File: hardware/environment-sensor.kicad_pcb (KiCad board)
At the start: 2 copper layers, 111 x 86 mm, 109 parts, among them P2 ICSP, P4 JTAG, P5 RB1-125BAG1A, P6 NSL-19M51, P7 PPD42, P8 POWER, SW1 Reset, U1 ATMEGA32U4-AU, U2 W5500, U3 Bosch_BME280, U4 LM317T, U5 LM317T, X1 16MHz, X2 25MHz

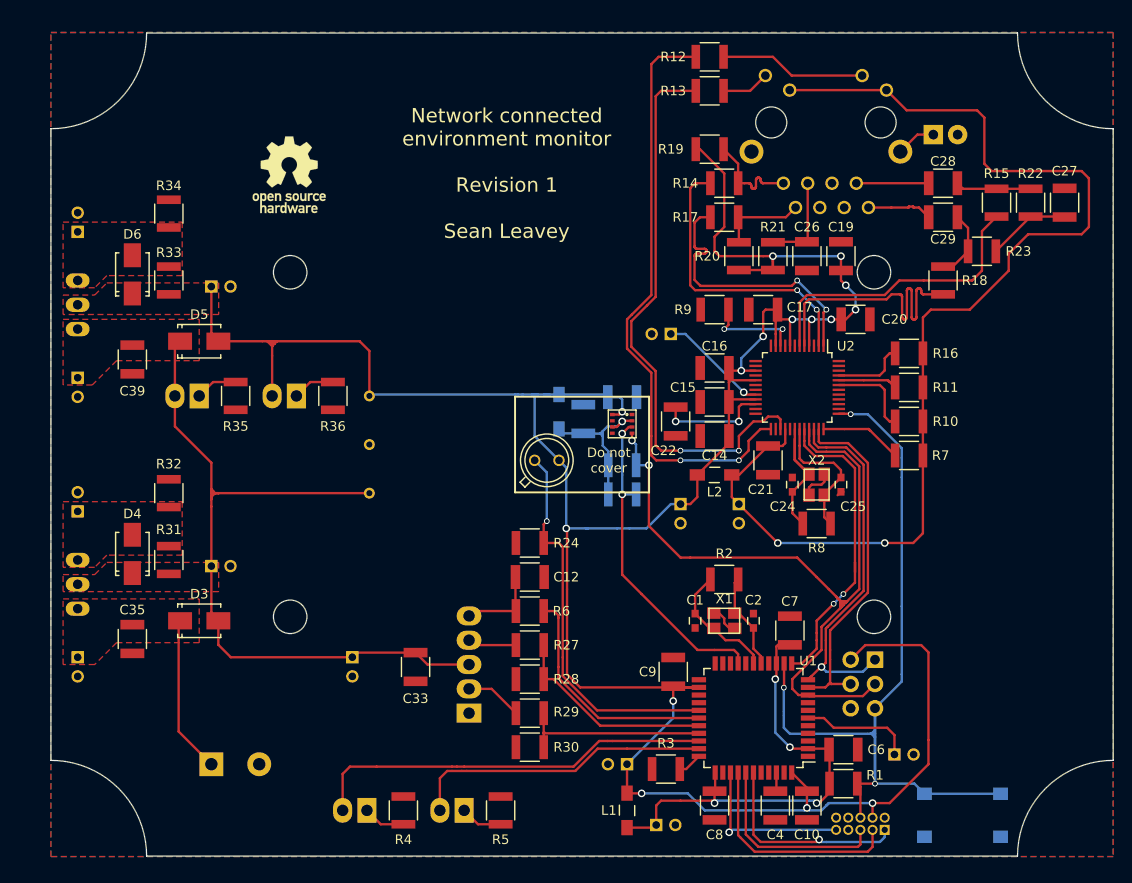
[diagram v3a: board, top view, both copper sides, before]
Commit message: Revision of board to address issues
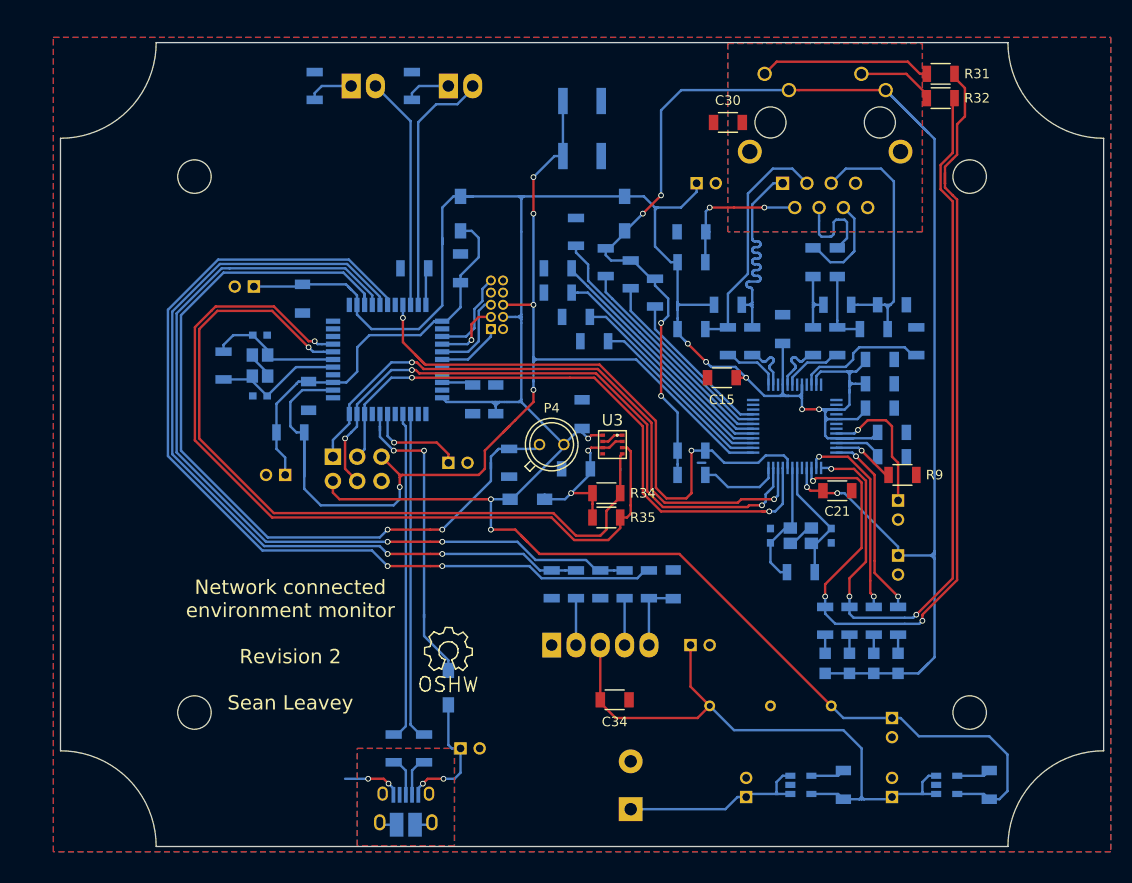
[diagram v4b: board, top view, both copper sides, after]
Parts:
- removed C40, C41: 10u, Capacitors_ThroughHole:C_Radial_D5_L11_P2
- removed D7: LED_5V, Connectors_Molex:Molex_KK-6410-02_02x2.54mm_Straight
- removed D8: LED_3V3, Connectors_Molex:Molex_KK-6410-02_02x2.54mm_Straight
- removed JP1: Shield ground, Pin_Headers:Pin_Header_Straight_1x02
- removed P7: PPD42, Connectors_Molex:Molex_KK-6410-05_05x2.54mm_Straight
- removed P8: POWER, Terminal_Blocks:TerminalBlock_Pheonix_MKDS1.5-2pol
- removed REF*** (x2): OSHW-Logo_7.5x8mm_SilkScreen, Symbols:OSHW-Logo_7.5x8mm_SilkScreen
- removed the Ref** at (156.8, 101.0)
- added J1: J1B1211CCD, Cetus_RJ45:Cetus_J1B1211CCD, B.Cu at (182.2, 67.3)
- added L4: Wurth WE-CBF, Choke_SMD:Choke_SMD_1206_Standard, B.Cu at (151.1, 106.7)
- added P1: USB_OTG, Connect:USB_Micro-B_10103594-0001LF, B.Cu at (138.4, 139.1)
- added P3: JTAG, Pin_Headers:Pin_Header_Straight_2x05_Pitch1.27mm, B.Cu at (147.3, 88.9)
- added R37: 10k, Resistors_SMD:R_1206, B.Cu at (158.8, 115.6)
- added R38: 10k, Resistors_SMD:R_1206, B.Cu at (156.2, 115.6)
- added R39: 10k, Resistors_SMD:R_1206, B.Cu at (153.7, 115.6)
- added R40: 330R, Resistors_SMD:R_1206, B.Cu at (184.8, 119.4)
- added R41: 330R, Resistors_SMD:R_1206, B.Cu at (189.9, 119.4)
- added R42: 330R, Resistors_SMD:R_1206, B.Cu at (187.3, 119.4)
- added R43: 330R, Resistors_SMD:R_1206, B.Cu at (182.2, 119.4)
- added REF**: Symbol_OSHW-Logo_SilkScreen, Symbols:Symbol_OSHW-Logo_SilkScreen, F.Cu at (142.9, 122.6)
- added Ref**: Val**, Board_Outlines:109mmx84mm_holes_b, F.Cu at (156.8, 101.0)
- C1: value 12p -> 10u; footprint Capacitors_SMD:C_0603 -> Capacitors_ThroughHole:C_Radial_D5_L11_P2; moved to B.Cu
- C10, C12, C14, C16, C17, C19, C20, C22, C27, C7, C8, C9: footprint Capacitors_SMD:C_1210 -> Capacitors_SMD:C_1206; moved to B.Cu
- C15, C21, C31: footprint Capacitors_SMD:C_1210 -> Capacitors_SMD:C_1206
- C2, L1, L2, U1, U2, X1, X2: moved to B.Cu
- C24, C25: value 12p -> 10p; moved to B.Cu
- C26: value 100n -> 22n; footprint Capacitors_SMD:C_1210 -> Capacitors_SMD:C_1206; moved to B.Cu
- C28, C29: value 10n -> 6.8n; footprint Capacitors_SMD:C_1210 -> Capacitors_SMD:C_1206; moved to B.Cu
- C3: value 10u -> 12p; footprint Capacitors_ThroughHole:C_Radial_D5_L11_P2 -> Capacitors_SMD:C_0603
- C30: value 100n -> 1n/2kV; footprint Capacitors_SMD:C_1210 -> Capacitors_SMD:C_1206; moved to F.Cu
- C32, C5: value 10u -> 100n; footprint Capacitors_ThroughHole:C_Radial_D5_L11_P2 -> Capacitors_SMD:C_1206
- C33, C35, C39, C6: value 100n -> 10u; footprint Capacitors_SMD:C_1210 -> Capacitors_ThroughHole:C_Radial_D5_L11_P2; moved to B.Cu
- C34: value 10u -> 100n; footprint Capacitors_ThroughHole:C_Radial_D5_L11_P2 -> Capacitors_SMD:C_1206; moved to F.Cu
- C36, C38: value 10u -> 10n; footprint Capacitors_ThroughHole:C_Radial_D5_L11_P2 -> Capacitors_SMD:C_1206
- C4: value 100n -> 1u; footprint Capacitors_SMD:C_1210 -> Capacitors_ThroughHole:C_Radial_D5_L11_P2; moved to B.Cu
- D3: value S1B-13-F -> LINKLED; footprint Diodes_SMD:SMA_Standard -> LEDs:LED_0805; moved to B.Cu
- D4: value S1B-13-F -> SPDLED; footprint Diodes_SMD:SMA_Standard -> LEDs:LED_0805; moved to B.Cu
- D5: value S1B-13-F -> DUPLED; footprint Diodes_SMD:SMA_Standard -> LEDs:LED_0805; moved to B.Cu
- D6: value S1B-13-F -> ACTLED; footprint Diodes_SMD:SMA_Standard -> LEDs:LED_0805; moved to B.Cu
- P4: value JTAG -> NSL-19M51; footprint Pin_Headers:Pin_Header_Straight_2x05_Pitch1.27mm -> TO_SOT_Packages_THT:TO-18_2Pin; moved to F.Cu
- P5: value RB1-125BAG1A -> PPD42; footprint Wiznet_RJ45:WIZNET_RB1-125BAG1A -> Connectors_Molex:Molex_KK-6410-05_05x2.54mm_Straight
- P6: value NSL-19M51 -> POWER; footprint TO_SOT_Packages_THT:TO-18_2Pin -> Terminal_Blocks:TerminalBlock_Pheonix_MKDS1.5-2pol; moved to B.Cu
- R1, R10, R11: footprint Resistors_SMD:R_1210 -> Resistors_SMD:R_1206; moved to B.Cu
- R12: value 330R -> 1M; footprint Resistors_SMD:R_1210 -> Resistors_SMD:R_1206; moved to B.Cu
- R13: value 330R -> 12k4/1%; footprint Resistors_SMD:R_1210 -> Resistors_SMD:R_1206; moved to B.Cu
- R14, R15, R18: value 33R -> 10k; footprint Resistors_SMD:R_1210 -> Resistors_SMD:R_1206; moved to B.Cu
- R16, R24: value 10k -> 0R; footprint Resistors_SMD:R_1210 -> Resistors_SMD:R_1206; moved to B.Cu
- R17: value 33R -> 0R; footprint Resistors_SMD:R_1210 -> Resistors_SMD:R_1206; moved to B.Cu
- R19, R20, R22, R23: value 49R9/1% -> 10k; footprint Resistors_SMD:R_1210 -> Resistors_SMD:R_1206; moved to B.Cu
- R2: value 1M -> 22R; footprint Resistors_SMD:R_1210 -> Resistors_SMD:R_1206; moved to B.Cu
- R21: value 10R/1% -> 10k; footprint Resistors_SMD:R_1210 -> Resistors_SMD:R_1206; moved to B.Cu
- R25: value 4k7 -> 0R; footprint Resistors_SMD:R_1210 -> Resistors_SMD:R_1206
- R26: value 4k7 -> 49R9/1%; footprint Resistors_SMD:R_1210 -> Resistors_SMD:R_1206
- R27, R29, R30: value 10k -> 49R9/1%; footprint Resistors_SMD:R_1210 -> Resistors_SMD:R_1206; moved to B.Cu
- R28: value 10k -> 10R/1%; footprint Resistors_SMD:R_1210 -> Resistors_SMD:R_1206; moved to B.Cu
- R3: value 10k -> 22R; footprint Resistors_SMD:R_1210 -> Resistors_SMD:R_1206; moved to B.Cu
- R31: value 110R -> 330R; footprint Resistors_SMD:R_1210 -> Resistors_SMD:R_1206
- R32: footprint Resistors_SMD:R_1210 -> Resistors_SMD:R_1206
- R33: value 110R -> 10k; footprint Resistors_SMD:R_1210 -> Resistors_SMD:R_1206; moved to B.Cu
- R34: value 180R -> 4k7; footprint Resistors_SMD:R_1210 -> Resistors_SMD:R_1206
- R35: value 270R -> 4k7; footprint Resistors_SMD:R_1210 -> Resistors_SMD:R_1206
- R36, R5: value 180R -> 10k; footprint Resistors_SMD:R_1210 -> Resistors_SMD:R_1206; moved to B.Cu
- R4: value 180R -> 1M; footprint Resistors_SMD:R_1210 -> Resistors_SMD:R_1206; moved to B.Cu
- R6, R7: value 10k -> 180R; footprint Resistors_SMD:R_1210 -> Resistors_SMD:R_1206; moved to B.Cu
- R8: value 1M -> 10k; footprint Resistors_SMD:R_1210 -> Resistors_SMD:R_1206; moved to B.Cu
- R9: value 12k4/1% -> 10k; footprint Resistors_SMD:R_1210 -> Resistors_SMD:R_1206
- SW1: footprint Buttons_Switches_SMD:SW_SPST_B3S-1000 -> Buttons_Switches_SMD:SW_SPST_B3SL-1002P
- U4: value LM317T -> LT1761-5; footprint TO_SOT_Packages_THT:TO-220_Neutral123_Vertical -> TO_SOT_Packages_SMD:SOT-23-5
- U5: value LM317T -> LT1761-3.3; footprint TO_SOT_Packages_THT:TO-220_Neutral123_Vertical -> TO_SOT_Packages_SMD:SOT-23-5
- moved C38 104.3 mm to (199.4, 136.5)
- moved U5 103.7 mm to (194.9, 136.5), turned to 0 degrees
- moved R31 95.3 mm to (194.3, 62.2), turned to 0 degrees
- moved R32 90.6 mm to (194.3, 64.8), turned to 0 degrees
- moved C39 87.8 mm to (189.2, 129.5)
- moved C36 85.0 mm to (184.2, 136.5), turned to 270 degrees
- moved D6 83.0 mm to (182.2, 123.8), turned to 270 degrees
- moved SW1 82.0 mm to (156.8, 67.9), turned to 270 degrees
- moved D4 80.8 mm to (189.9, 123.8), turned to 270 degrees
- moved U4 78.4 mm to (179.7, 136.5), turned to 0 degrees
- moved D5 78.1 mm to (187.3, 123.8), turned to 270 degrees
- moved C3 76.1 mm to (123.2, 95.9), turned to 180 degrees
- moved D1 75.7 mm to (132.7, 63.5), turned to 0 degrees
- moved D2 75.7 mm to (142.9, 63.5), turned to 0 degrees
- moved C37 75.1 mm to (189.2, 137.8), turned to 90 degrees
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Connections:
- net /Microcontroller/MISO renamed /Microcontroller/SPI_MISO
- net /Microcontroller/MOSI renamed /Microcontroller/SPI_MOSI
- C30 pad 1: /Microcontroller/3V3A -> GND
- C30 pad 2: GND -> /Network I/O/CHGND
- C31 pad 1: /Sensors/3V3D -> /Microcontroller/3V3A
- C32 pad 1: /Power Supply/5VA -> /Sensors/3V3D
- C33 pad 1: GND -> /Power Supply/5VA
- C33 pad 2: /Power Supply/5VA -> GND
- C34 pad 1: /Power Supply/+6V -> GND
- C34 pad 2: GND -> /Power Supply/5VA
- C36 pad 2: GND -> /Power Supply/5VA
- C38 pad 1: /Power Supply/5VA -> Net-(C38-Pad1)
- C38 pad 2: GND -> /Microcontroller/3V3A
- C39 pad 1: /Power Supply/5VA -> /Microcontroller/3V3A
- C5 pad 1: /Microcontroller/3V3D -> Net-(C5-Pad1)
- C6 pad 1: GND -> /Microcontroller/3V3D
- C6 pad 2: /Microcontroller/3V3D -> GND
- D3 pad 1: /Power Supply/+6V -> Net-(D3-Pad1)
- D3 pad 2: /Power Supply/5VA -> /Network I/O/3V3D
- D4 pad 1: /Power Supply/5VA -> Net-(D4-Pad1)
- D4 pad 2: Net-(C36-Pad1) -> /Network I/O/3V3D
- D5 pad 1: /Power Supply/5VA -> Net-(D5-Pad1)
- D5 pad 2: /Microcontroller/3V3A -> /Network I/O/3V3D
- D6 pad 1: /Microcontroller/3V3A -> Net-(D6-Pad1)
- D6 pad 2: Net-(C40-Pad1) -> /Network I/O/3V3D
- L2 pad 1: /Microcontroller/3V3A -> Net-(C1-Pad1)
- L2 pad 2: /Network I/O/3V3D -> Net-(L2-Pad2)
- L3 pad 2: /Sensors/3V3D -> /Network I/O/3V3D
- P2 pad 3: /Microcontroller/SCLK -> /Microcontroller/SPI_SCLK
- P4 pad 1: Net-(P4-Pad1) -> /Microcontroller/3V3A
- P4 pad 2: GND -> /Microcontroller/LDR_OUT
- P6 pad 1: /Microcontroller/3V3A -> /Power Supply/+6V
- P6 pad 2: /Microcontroller/LDR_OUT -> GND
- R10 pad 2: Net-(R10-Pad2) -> /Microcontroller/SS_PHY
- R12 pad 1: /Network I/O/LINKLED -> Net-(C24-Pad2)
- R12 pad 2: Net-(R12-Pad2) -> Net-(C25-Pad2)
- R13 pad 1: /Network I/O/ACTLED -> GND
- R14 pad 1: /Network I/O/TX1+ -> /Network I/O/3V3D
- R14 pad 2: /Network I/O/TX+ -> Net-(R14-Pad2)
- R15 pad 1: /Network I/O/RX1+ -> /Network I/O/3V3D
- R15 pad 2: /Network I/O/RX+ -> Net-(R15-Pad2)
- R16 pad 1: /Network I/O/3V3D -> /Network I/O/TX1+
- R16 pad 2: Net-(R16-Pad2) -> /Network I/O/TX+
- R17 pad 1: /Network I/O/TX1- -> /Network I/O/RX1+
- R17 pad 2: /Network I/O/TX- -> /Network I/O/RX+
- R18 pad 1: /Network I/O/RX1- -> GND
- R18 pad 2: /Network I/O/RX- -> Net-(R18-Pad2)
- R19 pad 1: /Network I/O/TX1+ -> GND
- R19 pad 2: /Microcontroller/3V3A -> Net-(R19-Pad2)
- R2 pad 1: Net-(C1-Pad1) -> /Microcontroller/USBD1+
- R2 pad 2: Net-(C2-Pad1) -> /Microcontroller/USBD+
- R20 pad 1: /Network I/O/TX1- -> GND
- R20 pad 2: /Microcontroller/3V3A -> Net-(R20-Pad2)
- R21 pad 1: Net-(C26-Pad1) -> GND
- R21 pad 2: /Microcontroller/3V3A -> Net-(R21-Pad2)
- R22 pad 1: Net-(C27-Pad1) -> GND
- R22 pad 2: /Network I/O/RX1+ -> Net-(R22-Pad2)
- R23 pad 1: Net-(C27-Pad1) -> /Network I/O/3V3D
- R23 pad 2: /Network I/O/RX1- -> Net-(R23-Pad2)
- R24 pad 1: /Microcontroller/LDR_OUT -> /Network I/O/TX1-
- R24 pad 2: GND -> /Network I/O/TX-
- R25 pad 1: /Sensors/3V3D -> /Network I/O/RX1-
- R25 pad 2: /Microcontroller/SCLK -> /Network I/O/RX-
- R26 pad 1: /Sensors/3V3D -> /Network I/O/TX1+
- R26 pad 2: /Microcontroller/SDA -> /Microcontroller/3V3A
- R27 pad 1: /Microcontroller/P_OUT_1 -> /Network I/O/TX1-
- R27 pad 2: Net-(P7-Pad4) -> /Microcontroller/3V3A
- R28 pad 1: GND -> Net-(C26-Pad1)
- R28 pad 2: /Microcontroller/P_OUT_1 -> /Microcontroller/3V3A
- R29 pad 1: /Microcontroller/P_OUT_2 -> Net-(C27-Pad1)
- R29 pad 2: Net-(P7-Pad2) -> /Network I/O/RX1+
- R3 pad 1: GND -> /Microcontroller/USBD1-
- R3 pad 2: Net-(R3-Pad2) -> /Microcontroller/USBD-
- R30 pad 1: GND -> Net-(C27-Pad1)
- R30 pad 2: /Microcontroller/P_OUT_2 -> /Network I/O/RX1-
- R31 pad 1: /Power Supply/5VA -> Net-(J1-Pad9)
- R31 pad 2: Net-(C36-Pad1) -> /Network I/O/ACTLED
- R32 pad 1: Net-(C36-Pad1) -> Net-(J1-Pad11)
- R32 pad 2: GND -> /Network I/O/LINKLED
- R33 pad 1: /Microcontroller/3V3A -> /Microcontroller/LDR_OUT
- R33 pad 2: Net-(C40-Pad1) -> GND
- R34 pad 1: Net-(C40-Pad1) -> /Sensors/3V3D
- R34 pad 2: GND -> /Microcontroller/I2C_SCLK
- R35 pad 1: Net-(D7-Pad1) -> /Sensors/3V3D
- R35 pad 2: GND -> /Microcontroller/I2C_SDA
- R36 pad 1: Net-(D8-Pad1) -> /Microcontroller/P_OUT_1
- R36 pad 2: GND -> Net-(P5-Pad4)
- R4 pad 1: GND -> Net-(C2-Pad1)
- R4 pad 2: Net-(D1-Pad1) -> Net-(C3-Pad1)
- R5 pad 2: Net-(D2-Pad1) -> Net-(R5-Pad2)
- R6 pad 1: /Microcontroller/P_THRESH -> GND
- R6 pad 2: Net-(R6-Pad2) -> Net-(D1-Pad1)
- R7 pad 1: /Network I/O/3V3D -> GND
- R7 pad 2: Net-(R7-Pad2) -> Net-(D2-Pad1)
- R8 pad 1: Net-(C24-Pad2) -> /Microcontroller/P_THRESH
- R8 pad 2: Net-(C25-Pad2) -> Net-(R8-Pad2)
- R9 pad 1: GND -> Net-(R9-Pad1)
- R9 pad 2: Net-(R9-Pad2) -> GND
- U1 pad 12: /Microcontroller/SS_PHY -> Net-(U1-Pad12)
- U1 pad 16: Net-(C2-Pad1) -> Net-(C3-Pad1)
- U1 pad 17: Net-(C1-Pad1) -> Net-(C2-Pad1)
- U1 pad 18: Net-(U1-Pad18) -> /Microcontroller/I2C_SCLK
- U1 pad 19: /Microcontroller/SDA -> /Microcontroller/I2C_SDA
- U1 pad 2: /Microcontroller/3V3D -> Net-(U1-Pad2)
- U1 pad 25: Net-(U1-Pad25) -> /Microcontroller/LDR_OUT
- U1 pad 26: Net-(U1-Pad26) -> /Microcontroller/P_OUT_1
- U1 pad 27: /Microcontroller/LDR_OUT -> /Microcontroller/P_OUT_2
- U1 pad 28: Net-(R6-Pad2) -> Net-(R8-Pad2)
- U1 pad 29: /Microcontroller/P_OUT_1 -> Net-(U1-Pad29)
- U1 pad 3: Net-(U1-Pad3) -> /Microcontroller/USBD1-
- U1 pad 30: /Microcontroller/P_OUT_2 -> /Microcontroller/SS_PHY
- U1 pad 33: Net-(R3-Pad2) -> Net-(R5-Pad2)
- U1 pad 36: Net-(P4-Pad9) -> Net-(P3-Pad9)
- U1 pad 37: Net-(P4-Pad3) -> Net-(P3-Pad3)
- U1 pad 38: Net-(P4-Pad5) -> Net-(P3-Pad5)
- U1 pad 39: Net-(P4-Pad1) -> Net-(P3-Pad1)
- U1 pad 4: Net-(U1-Pad4) -> /Microcontroller/USBD1+
- U1 pad 42: Net-(C4-Pad1) -> Net-(C5-Pad1)
- U1 pad 6: Net-(C3-Pad1) -> Net-(C4-Pad1)
- U1 pad 7: Net-(U1-Pad7) -> Net-(L2-Pad2)
- U1 pad 9: /Microcontroller/SCLK -> /Microcontroller/SPI_SCLK
- U2 pad 10: Net-(R9-Pad2) -> Net-(R13-Pad2)
- U2 pad 23: Net-(U2-Pad23) -> Net-(R9-Pad1)
- U2 pad 24: Net-(U2-Pad24) -> /Network I/O/SPDLED
- U2 pad 25: Net-(R12-Pad2) -> /Network I/O/LINKLED
- U2 pad 26: Net-(U2-Pad26) -> /Network I/O/DUPLED
- U2 pad 27: Net-(R13-Pad2) -> /Network I/O/ACTLED
- U2 pad 33: /Microcontroller/SCLK -> /Microcontroller/SPI_SCLK
- U2 pad 36: Net-(R7-Pad2) -> Net-(R11-Pad2)
- U2 pad 38: Net-(U2-Pad38) -> Net-(R18-Pad2)
- U2 pad 39: Net-(U2-Pad39) -> Net-(R19-Pad2)
- U2 pad 40: Net-(U2-Pad40) -> Net-(R20-Pad2)
- U2 pad 41: Net-(U2-Pad41) -> Net-(R21-Pad2)
- U2 pad 42: Net-(U2-Pad42) -> Net-(R22-Pad2)
- U2 pad 43: Net-(R10-Pad2) -> Net-(R14-Pad2)
- U2 pad 44: Net-(R11-Pad2) -> Net-(R15-Pad2)
- U2 pad 45: Net-(R16-Pad2) -> Net-(R23-Pad2)
- U3 pad 3: /Microcontroller/SDA -> /Microcontroller/I2C_SDA
- U3 pad 4: /Microcontroller/SCLK -> /Microcontroller/I2C_SCLK
- U4 pad 1: Net-(C36-Pad1) -> /Power Supply/+6V
- U4 pad 2: /Power Supply/5VA -> GND
- U5 pad 1: Net-(C40-Pad1) -> /Power Supply/5VA
- U5 pad 2: /Microcontroller/3V3A -> GND
- X1 pad 1: Net-(C1-Pad1) -> Net-(C2-Pad1)
- X1 pad 2: Net-(C2-Pad1) -> Net-(C3-Pad1)
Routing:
- net Net-(R8-Pad2): track 0.00 -> 98.7 mm, vias 0 -> 2
- net /Network I/O/ACTLED: track 5.03 -> 94.8 mm, vias 0 -> 3
- net /Microcontroller/I2C_SDA: track 0.00 -> 88.0 mm, vias 0 -> 1
- net /Microcontroller/I2C_SCLK: track 0.00 -> 83.6 mm, vias 0 -> 1
- net /Microcontroller/SCLK: track 82.3 -> 0.00 mm, vias 2 -> 0
- net /Microcontroller/P_OUT_1: track 21.8 -> 91.0 mm, vias 0 -> 2
- net /Network I/O/LINKLED: track 15.3 -> 84.2 mm, vias 0 -> 3
- net /Microcontroller/P_OUT_2: track 20.0 -> 88.1 mm, vias 0 -> 2
- net /Microcontroller/SPI_SCLK: track 0.00 -> 64.8 mm, vias 0 -> 2
- net Net-(R12-Pad2): track 62.6 -> 0.00 mm, vias 2 -> 0
- net /Network I/O/3V3D: track 121.0 -> 172.6 mm, vias 2 -> 6
- net Net-(R13-Pad2): track 59.8 -> 13.9 mm, vias 2 -> 0
- net /Microcontroller/LDR_OUT: track 40.7 -> 86.0 mm, vias 1 -> 2
- net /Microcontroller/USBD1+: track 0.00 -> 34.4 mm
- net /Microcontroller/USBD1-: track 0.00 -> 34.3 mm
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- added copper zone on B.Cu, net /Network I/O/CHGND
- added copper zone on F.Cu, net /Network I/O/CHGND
- added copper zone on B.Cu, net Net-(P1-Pad6)
- added copper zone on F.Cu, net Net-(P1-Pad6)
- removed copper zone on F.Cu, net /Microcontroller/3V3A
- removed copper zone on F.Cu, net /Power Supply/+6V
- removed copper zone on F.Cu, net /Power Supply/5VA
- removed copper zone on F.Cu, net Net-(C36-Pad1)
- removed copper zone on F.Cu, net Net-(C40-Pad1)
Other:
- board size 111 x 86 mm -> 109 x 84 mm
- net class HF Signal removed
- net class LF Signal removed
- net class Power: trace_width 0.25 -> 0.254; via_dia 0.8 -> 0.6; via_drill 0.5 -> 0.4
- net class Signal added: clearance 0.2, trace_width 0.254, via_dia 0.6, via_drill 0.4
- net class Unused removed
- rule pad_to_mask_clearance: 0.2 -> 0
- board text added: "6V"
- board text added: "Network connected environment monitor Revision 2 Sean Leavey"
- board text removed: "+6V"
- board text removed: "1"
- board text removed: "3.3V On"
- board text removed: "5V On"
- board text removed: "Do not cover"
- board text removed: "Network connected environment monitor Revision 1 Sean Leavey"
- board text removed: "RJ45 shield ground"
- board text removed: "Reset"

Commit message: Small update to board
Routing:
- net /Network I/O/3V3D: track 172.6 -> 164.7 mm, vias 6 -> 7
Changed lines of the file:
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@@
-(kicad_pcb (version 4) (host pcbnew 4.0.4+dfsg1-stable)
+(kicad_pcb (version 4) (host pcbnew 4.0.2+dfsg1-stable)
   (general
     (links 258)
     (no_connects 0)
-    (area 101.6 56.144999 212.090001 143.740001)
+    (area 102.132499 56.144999 211.557501 143.740001)
     (thickness 1.6)
     (drawings 22)
-    (tracks 1222)
+    (tracks 1212)
     (zones 0)
     (modules 112)
@@
     (visible_elements FFFFFF7F)
     (pcbplotparams
-      (layerselection 0x00030_80000001)
+      (layerselection 0x010f0_80000001)
       (usegerberextensions false)
       (excludeedgelayer true)
@@
       (outputformat 1)
       (mirror false)
-      (drillshape 1)
+      (drillshape 0)
       (scaleselection 1)
-      (outputdirectory ""))
+      (outputdirectory manufacturing/2017-06-21))
   )
   (net 0 "")
@@
   (segment (start 163.83 117.02) (end 166.32 117.02) (width 0.254) (layer B.Cu) (net 9))
   (segment (start 166.32 117.02) (end 166.37 117.07) (width 0.254) (layer B.Cu) (net 9))
-  (segment (start 193.675 112.268) (end 193.675 112.141) (width 0.254) (layer B.Cu) (net 10))
-  (segment (start 193.675 112.141) (end 193.675 69.035) (width 0.254) (layer B.Cu) (net 10))
-  (segment (start 193.326 112.554) (end 193.675 112.205) (width 0.254) (layer B.Cu) (net 10))
-  (segment (start 193.675 112.205) (end 193.675 112.141) (width 0.254) (layer B.Cu) (net 10))
-  (segment (start 193.675 123.19) (end 193.675 112.903) (width 0.254) (layer B.Cu) (net 10))
-  (segment (start 193.326 112.554) (end 193.675 112.903) (width 0.254) (layer B.Cu) (net 10))
-  (segment (start 193.675 112.903) (end 193.675 112.395) (width 0.254) (layer B.Cu) (net 10))
-  (segment (start 193.294 112.554) (end 193.326 112.554) (width 0.254) (layer B.Cu) (net 10))
-  (segment (start 193.294 112.554) (end 193.516 112.554) (width 0.254) (layer B.Cu) (net 10))
-  (segment (start 193.294 112.554) (end 193.389 112.554) (width 0.254) (layer B.Cu) (net 10))
-  (segment (start 189.865 112.554) (end 193.294 112.554) (width 0.254) (layer B.Cu) (net 10))
-  (segment (start 193.675 112.395) (end 193.675 112.268) (width 0.254) (layer B.Cu) (net 10))
-  (segment (start 193.389 112.554) (end 193.675 112.268) (width 0.254) (layer B.Cu) (net 10))
-  (segment (start 193.516 112.554) (end 193.675 112.395) (width 0.254) (layer B.Cu) (net 10))
-  (segment (start 193.675 69.035) (end 188.57 63.93) (width 0.254) (layer B.Cu) (net 10))
+  (segment (start 193.675 112.395) (end 193.675 69.035) (width 0.254) (layer F.Cu) (net 10))
+  (segment (start 193.675 69.035) (end 188.57 63.93) (width 0.254) (layer F.Cu) (net 10))
+  (segment (start 193.675 112.395) (end 190.024 112.395) (width 0.254) (layer F.Cu) (net 10))
+  (segment (start 190.024 112.395) (end 189.865 112.554) (width 0.254) (layer F.Cu) (net 10))
+  (segment (start 193.675 123.19) (end 193.675 112.395) (width 0.254) (layer B.Cu) (net 10))
+  (via (at 193.675 112.395) (size 0.6) (drill 0.4) (layers F.Cu B.Cu) (net 10))
   (segment (start 191.99098 124.87402) (end 193.675 123.19) (width 0.254) (layer B.Cu) (net 10))
   (segment (start 189.865 112.554) (end 189.865 111.65) (width 0.254) (layer B.Cu) (net 10))
@@
   (segment (start 189.865 124.87402) (end 191.99098 124.87402) (width 0.254) (layer B.Cu) (net 10))
   (segment (start 191.99098 124.87402) (end 193.04 123.825) (width 0.254) (layer B.Cu) (net 10))
-  (segment (start 188.57 63.93) (end 193.04 68.4) (width 0.254) (layer B.Cu) (net 10))
   (segment (start 163.195 76.835) (end 161.39414 78.63586) (width 0.254) (layer B.Cu) (net 10))
   (segment (start 161.39414 78.63586) (end 161.29 78.63586) (width 0.254) (layer B.Cu) (net 10))
@@
   (segment (start 179.075471 93.050528) (end 178.969407 93.156593) (width 0.254) (layer B.Cu) (net 67))
   (segment (start 178.969407 93.156593) (end 178.32 93.806) (width 0.254) (layer B.Cu) (net 67))
+  (segment (start 196.034009 67.490991) (end 196.85 66.675) (width 0.254) (layer F.Cu) (net 68))
+  (segment (start 196.85 66.675) (end 196.85 63.72) (width 0.254) (layer F.Cu) (net 68))
+  (segment (start 196.85 63.72) (end 195.76 62.63) (width 0.254) (layer F.Cu) (net 68))
+  (segment (start 196.034009 70.673057) (end 196.034009 67.490991) (width 0.254) (layer F.Cu) (net 68))
+  (segment (start 195.583533 71.123533) (end 196.034009 70.673057) (width 0.254) (layer F.Cu) (net 68))
   (segment (start 195.583533 71.123533) (end 194.764002 71.943064) (width 0.254) (layer F.Cu) (net 68))
-  (segment (start 194.764002 73.66) (end 194.76401 73.66) (width 0.254) (layer F.Cu) (net 68))
   (segment (start 194.764002 71.943064) (end 194.764002 73.66) (width 0.254) (layer F.Cu) (net 68))
+  (segment (start 194.76401 73.66) (end 194.76401 72.57099) (width 0.254) (layer F.Cu) (net 68))
   (segment (start 195.587066 74.93) (end 194.76401 74.106944) (width 0.254) (layer F.Cu) (net 68))
-  (segment (start 196.034009 75.376943) (end 195.587066 74.93) (width 0.254) (layer F.Cu) (net 68))
   (segment (start 194.76401 74.106944) (end 194.76401 73.66) (width 0.254) (layer F.Cu) (net 68))
-  (segment (start 194.76401 73.66) (end 194.76401 72.57099) (width 0.254) (layer F.Cu) (net 68))
+  (segment (start 194.764002 73.66) (end 194.76401 73.66) (width 0.254) (layer F.Cu) (net 68))
+  (segment (start 196.034009 75.376943) (end 195.587066 74.93) (width 0.254) (layer F.Cu) (net 68))
+  (segment (start 196.034009 115.123057) (end 196.034009 75.376943) (width 0.254) (layer F.Cu) (net 68))
   (segment (start 192.405 119.38) (end 192.405 118.752066) (width 0.254) (layer F.Cu) (net 68))
   (segment (start 192.405 118.752066) (end 196.034009 115.123057) (width 0.254) (layer F.Cu) (net 68))
-  (segment (start 196.034009 115.123057) (end 196.034009 75.376943) (width 0.254) (layer F.Cu) (net 68))
-  (segment (start 196.85 66.675) (end 196.85 63.72) (width 0.254) (layer F.Cu) (net 68))
-  (segment (start 195.583533 71.123533) (end 196.034009 70.673057) (width 0.254) (layer F.Cu) (net 68))
-  (segment (start 196.034009 70.673057) (end 196.034009 67.490991) (width 0.254) (layer F.Cu) (net 68))
-  (segment (start 196.034009 67.490991) (end 196.85 66.675) (width 0.254) (layer F.Cu) (net 68))
-  (segment (start 196.85 63.72) (end 195.76 62.63) (width 0.254) (layer F.Cu) (net 68))
   (segment (start 195.76 62.63) (end 195.76 62.23) (width 0.254) (layer F.Cu) (net 68))
   (segment (start 190.5635 119.6975) (end 192.0875 119.6975) (width 0.254) (layer B.Cu) (net 68))
@@
   (segment (start 180.82 104.62) (end 180.975 104.775) (width 0.254) (layer B.Cu) (net 68))
   (via (at 180.975 104.775) (size 0.6) (drill 0.4) (layers F.Cu B.Cu) (net 68))
-  (segment (start 191.77 118.745) (end 195.58 114.935) (width 0.254) (layer F.Cu) (net 69))
-  (segment (start 195.58 114.935) (end 195.58 75.565) (width 0.254) (layer F.Cu) (net 69))
+  (segment (start 195.58 70.485) (end 195.58 64.95) (width 0.254) (layer F.Cu) (net 69))
+  (segment (start 194.31 71.755) (end 195.58 70.485) (width 0.254) (layer F.Cu) (net 69))
+  (segment (start 194.31 74.295) (end 194.31 71.755) (width 0.254) (layer F.Cu) (net 69))
   (segment (start 195.58 75.565) (end 194.31 74.295) (width 0.254) (layer F.Cu) (net 69))
+  (segment (start 195.58 114.935) (end 195.58 75.565) (width 0.254) (layer F.Cu) (net 69))
+  (segment (start 191.77 118.745) (end 195.58 114.935) (width 0.254) (layer F.Cu) (net 69))
   (segment (start 195.58 64.95) (end 195.76 64.77) (width 0.254) (layer F.Cu) (net 69))
-  (segment (start 194.31 74.295) (end 194.31 71.755) (width 0.254) (layer F.Cu) (net 69))
-  (segment (start 194.31 71.755) (end 195.58 70.485) (width 0.254) (layer F.Cu) (net 69))
-  (segment (start 195.58 70.485) (end 195.58 64.95) (width 0.254) (layer F.Cu) (net 69))
   (segment (start 190.5635 119.0625) (end 191.4525 119.0625) (width 0.254) (layer B.Cu) (net 69))
   (segment (start 191.4525 119.0625) (end 191.77 118.745) (width 0.254) (layer B.Cu) (net 69))
@@
     (connect_pads (clearance 0.1))
     (min_thickness 0.254)
-    (fill yes (arc_segments 16) (thermal_gap 0.508) (thermal_bridge_width 0.508) (smoothing fillet) (radius 10))
+    (fill yes (arc_segments 32) (thermal_gap 0.508) (thermal_bridge_width 0.508) (smoothing fillet) (radius 10))
     (polygon
       (pts
-        (xy 212.09 143.51) (xy 101.6 143.51) (xy 101.6 58.42) (xy 212.09 58.42)
+        (xy 211.455 142.875) (xy 102.235 142.875) (xy 102.235 59.055) (xy 211.455 59.055)
       )
     )
@@
     (polygon
       (pts
-        (xy 212.09 58.42) (xy 212.09 143.51) (xy 101.6 143.51) (xy 101.6 58.42)
+        (xy 211.455 59.055) (xy 211.455 142.875) (xy 102.235 142.875) (xy 102.235 59.055)
       )
     )
